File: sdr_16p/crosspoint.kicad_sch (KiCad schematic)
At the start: 2 parts, among them U47 SN74CBT16212CDL, U48 SN74CBT16212CDL

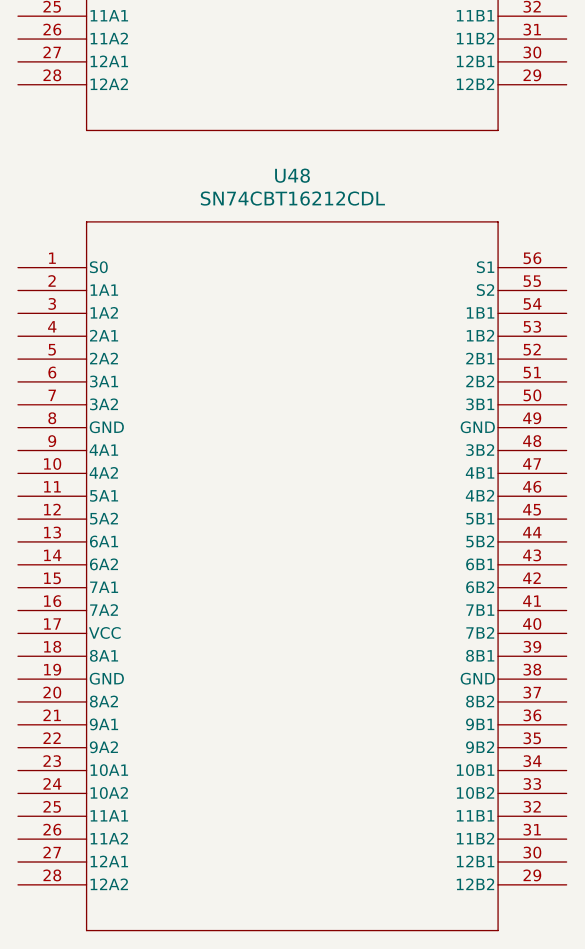
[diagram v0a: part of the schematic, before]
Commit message: back to 16 phases
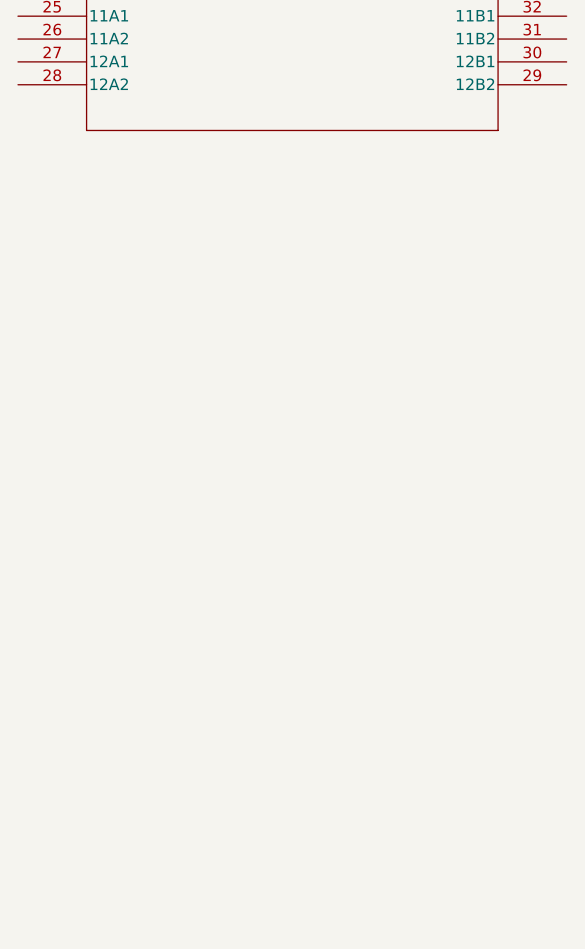
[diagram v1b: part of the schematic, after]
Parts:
- removed U48: SN74CBT16212CDL, DL56, symbol SN74CBT16212C:SN74CBT16212CDL
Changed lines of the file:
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@@
-	(symbol
-		(lib_id "SN74CBT16212C:SN74CBT16212CDL")
-		(at 201.93 128.27 0)
-		(unit 1)
-		(exclude_from_sim no)
-		(in_bom yes)
-		(on_board yes)
-		(dnp no)
-		(fields_autoplaced yes)
-		(property "Reference" "U48"
-			(at 232.41 118.11 0)
-			(effects
-				(font
-					(size 1.524 1.524)
-				)
-			)
-		)
-		(property "Value" "SN74CBT16212CDL"
-			(at 232.41 120.65 0)
-			(effects
-				(font
-					(size 1.524 1.524)
-				)
-			)
-		)
-		(property "Footprint" "DL56"
-			(at 201.93 128.27 0)
-			(effects
-				(font
-					(size 1.27 1.27)
-					(italic yes)
-				)
-				(hide yes)
-			)
-		)
-		(property "Datasheet" "https://www.ti.com/lit/gpn/sn74cbt16212c"
-			(at 201.93 128.27 0)
-			(effects
-				(font
-					(size 1.27 1.27)
-					(italic yes)
-				)
-				(hide yes)
-			)
-		)
-		(property "Description" ""
-			(at 201.93 128.27 0)
-			(effects
-				(font
-					(size 1.27 1.27)
-				)
-				(hide yes)
-			)
-		)
-		(pin "39"
-		)
-		(pin "43"
-		)
-		(pin "34"
-		)
-		(pin "18"
-		)
-		(pin "24"
-		)
-		(pin "37"
-		)
-		(pin "45"
-		)
-		(pin "11"
-		)
-		(pin "41"
-		)
-		(pin "44"
-		)
-		(pin "12"
-		)
-		(pin "46"
-		)
-		(pin "16"
-		)
-		(pin "25"
-		)
-		(pin "17"
-		)
-		(pin "47"
-		)
-		(pin "52"
-		)
-		(pin "35"
-		)
-		(pin "50"
-		)
-		(pin "19"
-		)
-		(pin "38"
-		)
-		(pin "29"
-		)
-		(pin "14"
-		)
-		(pin "48"
-		)
-		(pin "30"
-		)
-		(pin "33"
-		)
-		(pin "40"
-		)
-		(pin "6"
-		)
-		(pin "51"
-		)
-		(pin "26"
-		)
-		(pin "31"
-		)
-		(pin "49"
-		)
-		(pin "1"
-		)
-		(pin "4"
-		)
-		(pin "28"
-		)
-		(pin "54"
-		)
-		(pin "21"
-		)
-		(pin "23"
-		)
-		(pin "10"
-		)
-		(pin "15"
-		)
-		(pin "13"
-		)
-		(pin "56"
-		)
-		(pin "27"
-		)
-		(pin "55"
-		)
-		(pin "5"
-		)
-		(pin "42"
-		)
-		(pin "32"
-		)
-		(pin "20"
-		)
-		(pin "9"
-		)
-		(pin "8"
-		)
-		(pin "53"
-		)
-		(pin "22"
-		)
-		(pin "7"
-		)
-		(pin "3"
-		)
-		(pin "2"
-		)
-		(pin "36"
-		)
-		(instances
-			(project ""
-				(path "/fe42ca2f-2bb8-4d5a-9e84-807788ed632f/173d5eca-f61f-4af5-84ba-0d581841d6d2"
-					(reference "U48")
-					(unit 1)
-				)
-			)
-		)
-	)
 	(symbol
 		(lib_id "SN74CBT16212C:SN74CBT16212CDL")

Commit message: updated crosspoint
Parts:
- added C1: 10u, Capacitor_SMD:C_0603_1608Metric_Pad1.08x0.95mm_HandSolder, symbol Device:C_Small_US
- added C2, C3: 0.1u, Capacitor_SMD:C_0603_1608Metric_Pad1.08x0.95mm_HandSolder, symbol Device:C_Small_US
- added FB1: 600 ohm @100MHz, Max DCR=0.2, symbol Device:FerriteBead_Small
- added R1, R2: 10k, Resistor_SMD:R_0603_1608Metric_Pad0.98x0.95mm_HandSolder, symbol Device:R_Small_US
- added U1: SN74CBT16212CDL, DL56, symbol SN74CBT16212C:SN74CBT16212CDL
- renumbered U47 to U?
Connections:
- net S0_CTRL: now reaches U?.1 (S0)
- net S0_CTRL: now also R1.2, U1.1 (S0)
- net GND: now reaches U?.10 (4A2)
- net GND: now also U?.12 (5A2), U?.14 (6A2), U?.16 (7A2), U?.19 (GND), U?.20 (8A2), U?.22 (9A2), U?.24 (10A2), U?.26 (11A2), U?.28 (12A2), U?.3 (1A2), U?.38 (GND), U?.49 (GND), U?.5 (2A2), U?.55 (S2), U?.7 (3A2), U?.8 (GND), C1.2, C2.2, C3.2, R1.1, R2.2, U1.10 (4A2), U1.11 (5A1), U1.12 (5A2), U1.13 (6A1), U1.14 (6A2), U1.15 (7A1), U1.16 (7A2), U1.18 (8A1), U1.19 (GND), U1.20 (8A2), U1.21 (9A1), U1.22 (9A2), U1.23 (10A1), U1.24 (10A2), U1.25 (11A1), U1.26 (11A2), U1.27 (12A1), U1.28 (12A2), U1.29 (12B2), U1.3 (1A2), U1.30 (12B1), U1.31 (11B2), U1.32 (11B1), U1.33 (10B2), U1.34 (10B1), U1.35 (9B2), U1.36 (9B1), U1.37 (8B2), U1.38 (GND), U1.39 (8B1), U1.40 (7B2), U1.41 (7B1), U1.42 (6B2), U1.43 (6B1), U1.44 (5B2), U1.45 (5B1), U1.49 (GND), U1.5 (2A2), U1.55 (S2), U1.7 (3A2), U1.8 (GND)
- net Phase_4: now reaches U?.11 (5A1)
- net Phase_5: now reaches U?.13 (6A1)
- net Phase_6: now reaches U?.15 (7A1)
- net at U?.17 (VCC): now also C1.1, C2.1, C3.1, FB1.2, U1.17 (VCC)
- net Phase_7: now reaches U?.18 (8A1)
- net Phase_0: now reaches U?.2 (1A1)
- net Phase_8: now reaches U?.21 (9A1)
- net Phase_9: now reaches U?.23 (10A1)
- net Phase_10: now reaches U?.25 (11A1)
- net Phase_11: now reaches U?.27 (12A1)
- net Tx_Phase_11: now reaches U?.29 (12B2)
- net Rx_Phase_11: now reaches U?.30 (12B1)
- net Tx_Phase_10: now reaches U?.31 (11B2)
- net Rx_Phase_10: now reaches U?.32 (11B1)
- net Tx_Phase_9: now reaches U?.33 (10B2)
- net Rx_Phase_9: now reaches U?.34 (10B1)
- net Tx_Phase_8: now reaches U?.35 (9B2)
- net Rx_Phase_8: now reaches U?.36 (9B1)
- net Tx_Phase_7: now reaches U?.37 (8B2)
- net Rx_Phase_7: now reaches U?.39 (8B1)
- net Phase_1: now reaches U?.4 (2A1)
- net Tx_Phase_6: now reaches U?.40 (7B2)
- net Rx_Phase_6: now reaches U?.41 (7B1)
- net Tx_Phase_5: now reaches U?.42 (6B2)
- net Rx_Phase_5: now reaches U?.43 (6B1)
- net Tx_Phase_4: now reaches U?.44 (5B2)
- net Rx_Phase_4: now reaches U?.45 (5B1)
- net Tx_Phase_3: now reaches U?.46 (4B2)
- net Rx_Phase_3: now reaches U?.47 (4B1)
- net Tx_Phase_2: now reaches U?.48 (3B2)
- net Rx_Phase_2: now reaches U?.50 (3B1)
- net Tx_Phase_1: now reaches U?.51 (2B2)
- net Rx_Phase_1: now reaches U?.52 (2B1)
- net Tx_Phase_0: now reaches U?.53 (1B2)
- net Rx_Phase_0: now reaches U?.54 (1B1)
- net S1_CTRL: now reaches U?.56 (S1)
- net S1_CTRL: now also R2.1, U1.56 (S1)
- net Phase_2: now reaches U?.6 (3A1)
- net Phase_3: now reaches U?.9 (4A1)
- new net 5V_Crosspoint: FB1.1
- new net Phase_12: U1.2 (1A1)
- new net Phase_13: U1.4 (2A1)
- new net Phase_14: U1.6 (3A1)
- new net Phase_15: U1.9 (4A1)
- new net Rx_Phase_12: U1.54 (1B1)
- new net Rx_Phase_13: U1.52 (2B1)
- new net Rx_Phase_14: U1.50 (3B1)
- new net Rx_Phase_15: U1.47 (4B1)
- new net Tx_Phase_12: U1.53 (1B2)
- new net Tx_Phase_13: U1.51 (2B2)
- new net Tx_Phase_14: U1.48 (3B2)
- new net Tx_Phase_15: U1.46 (4B2)
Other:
- note added: "Place 0.1uF cap as close to VCC as possible"
- note added: "RP2040 should be able to drive S0 and S1 directly. A 10k pulldown is added just so the everything is disconnected if there is no signal from the RP2040"
- note added: "Receive: S0 = High, S1 = Low Transimit: S0 = Low, S1 = High Disconnect: S0 = Low, S1 = Low S2 is always Low"
- moved on the sheet: U?
